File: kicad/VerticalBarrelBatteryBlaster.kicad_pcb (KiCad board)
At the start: 2 copper layers, 21.1 x 10.3 mm, 3 parts

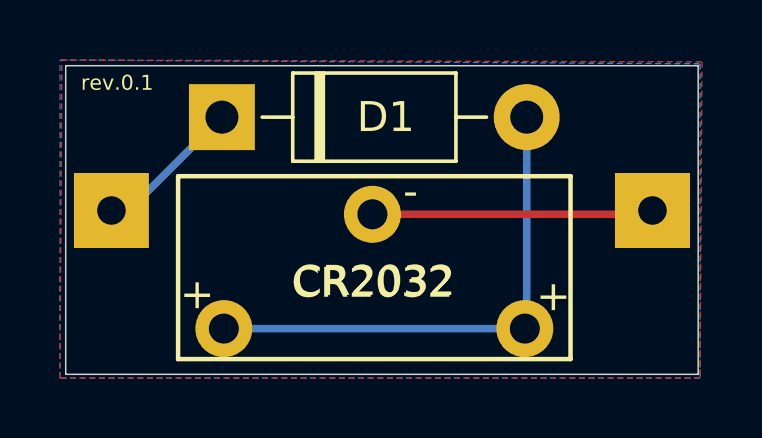
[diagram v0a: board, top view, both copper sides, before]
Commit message: Rev.0.2: Improves printed text
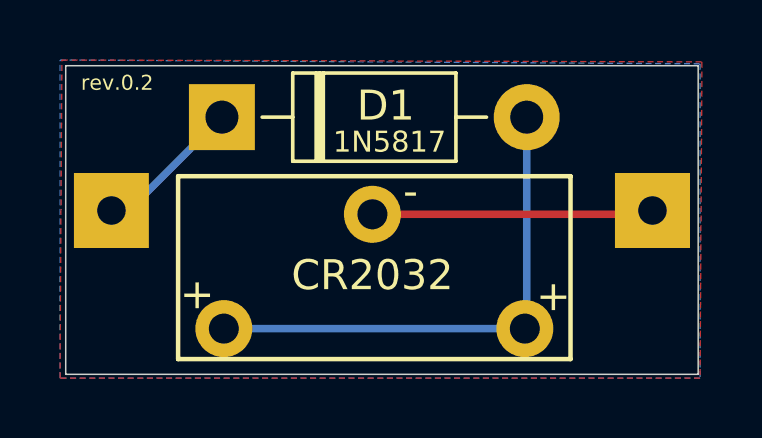
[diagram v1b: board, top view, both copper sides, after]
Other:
- board text added: "-"
- board text added: "1N5817"
- board text added: "rev.0.2"
- board text removed: "rev.0.1"
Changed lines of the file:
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@@
   (general
     (thickness 1.6)
-    (drawings 124)
+    (drawings 126)
     (tracks 7)
     (zones 0)
@@
     (descr "Diode, DO-41_SOD81 series, Axial, Horizontal, pin pitch=10.16mm, , length*diameter=5.2*2.7mm^2, , http://www.diodes.com/_files/packages/DO-41%20(Plastic).pdf")
     (tags "Diode DO-41_SOD81 series Axial Horizontal pin pitch 10.16mm  length 5.2mm diameter 2.7mm")
-    (fp_text reference D1 (at 5.461 0) (layer F.SilkS)
+    (fp_text reference D1 (at 5.461 -0.381) (layer F.SilkS)
       (effects (font (size 1 1) (thickness 0.15)))
     )
@@
       (effects (font (size 1 1) (thickness 0.15)))
     )
+    (fp_line (start 2.48 -1.35) (end 2.48 1.35) (layer F.Fab) (width 0.1))
+    (fp_line (start 2.48 1.35) (end 7.68 1.35) (layer F.Fab) (width 0.1))
+    (fp_line (start 7.68 1.35) (end 7.68 -1.35) (layer F.Fab) (width 0.1))
+    (fp_line (start 7.68 -1.35) (end 2.48 -1.35) (layer F.Fab) (width 0.1))
+    (fp_line (start 0 0) (end 2.48 0) (layer F.Fab) (width 0.1))
+    (fp_line (start 10.16 0) (end 7.68 0) (layer F.Fab) (width 0.1))
+    (fp_line (start 3.26 -1.35) (end 3.26 1.35) (layer F.Fab) (width 0.1))
+    (fp_line (start 3.36 -1.35) (end 3.36 1.35) (layer F.Fab) (width 0.1))
+    (fp_line (start 3.16 -1.35) (end 3.16 1.35) (layer F.Fab) (width 0.1))
+    (fp_line (start 2.36 -1.47) (end 2.36 1.47) (layer F.SilkS) (width 0.12))
+    (fp_line (start 2.36 1.47) (end 7.8 1.47) (layer F.SilkS) (width 0.12))
+    (fp_line (start 7.8 1.47) (end 7.8 -1.47) (layer F.SilkS) (width 0.12))
+    (fp_line (start 7.8 -1.47) (end 2.36 -1.47) (layer F.SilkS) (width 0.12))
+    (fp_line (start 1.34 0) (end 2.36 0) (layer F.SilkS) (width 0.12))
+    (fp_line (start 8.82 0) (end 7.8 0) (layer F.SilkS) (width 0.12))
+    (fp_line (start 3.26 -1.47) (end 3.26 1.47) (layer F.SilkS) (width 0.12))
+    (fp_line (start 3.38 -1.47) (end 3.38 1.47) (layer F.SilkS) (width 0.12))
+    (fp_line (start 3.14 -1.47) (end 3.14 1.47) (layer F.SilkS) (width 0.12))
+    (fp_line (start -1.35 -1.6) (end -1.35 1.6) (layer F.CrtYd) (width 0.05))
+    (fp_line (start -1.35 1.6) (end 11.51 1.6) (layer F.CrtYd) (width 0.05))
+    (fp_line (start 11.51 1.6) (end 11.51 -1.6) (layer F.CrtYd) (width 0.05))
     (fp_line (start 11.51 -1.6) (end -1.35 -1.6) (layer F.CrtYd) (width 0.05))
-    (fp_line (start 11.51 1.6) (end 11.51 -1.6) (layer F.CrtYd) (width 0.05))
-    (fp_line (start -1.35 1.6) (end 11.51 1.6) (layer F.CrtYd) (width 0.05))
-    (fp_line (start -1.35 -1.6) (end -1.35 1.6) (layer F.CrtYd) (width 0.05))
-    (fp_line (start 3.14 -1.47) (end 3.14 1.47) (layer F.SilkS) (width 0.12))
-    (fp_line (start 3.38 -1.47) (end 3.38 1.47) (layer F.SilkS) (width 0.12))
-    (fp_line (start 3.26 -1.47) (end 3.26 1.47) (layer F.SilkS) (width 0.12))
-    (fp_line (start 8.82 0) (end 7.8 0) (layer F.SilkS) (width 0.12))
-    (fp_line (start 1.34 0) (end 2.36 0) (layer F.SilkS) (width 0.12))
-    (fp_line (start 7.8 -1.47) (end 2.36 -1.47) (layer F.SilkS) (width 0.12))
-    (fp_line (start 7.8 1.47) (end 7.8 -1.47) (layer F.SilkS) (width 0.12))
-    (fp_line (start 2.36 1.47) (end 7.8 1.47) (layer F.SilkS) (width 0.12))
-    (fp_line (start 2.36 -1.47) (end 2.36 1.47) (layer F.SilkS) (width 0.12))
-    (fp_line (start 3.16 -1.35) (end 3.16 1.35) (layer F.Fab) (width 0.1))
-    (fp_line (start 3.36 -1.35) (end 3.36 1.35) (layer F.Fab) (width 0.1))
-    (fp_line (start 3.26 -1.35) (end 3.26 1.35) (layer F.Fab) (width 0.1))
-    (fp_line (start 10.16 0) (end 7.68 0) (layer F.Fab) (width 0.1))
-    (fp_line (start 0 0) (end 2.48 0) (layer F.Fab) (width 0.1))
-    (fp_line (start 7.68 -1.35) (end 2.48 -1.35) (layer F.Fab) (width 0.1))
-    (fp_line (start 7.68 1.35) (end 7.68 -1.35) (layer F.Fab) (width 0.1))
-    (fp_line (start 2.48 1.35) (end 7.68 1.35) (layer F.Fab) (width 0.1))
-    (fp_line (start 2.48 -1.35) (end 2.48 1.35) (layer F.Fab) (width 0.1))
     (fp_text user K (at -1.5875 -3.937) (layer F.SilkS) hide
       (effects (font (size 1 1) (thickness 0.15)))
@@
       (effects (font (size 1 1) (thickness 0.15)))
     )
-    (fp_text user %R (at 5.47 0) (layer F.Fab)
+    (fp_text user %R (at 5.47 -0.5715) (layer F.Fab)
       (effects (font (size 1 1) (thickness 0.15)))
     )
@@
   (module VerticalBarrelBatteryBlaster:cr2032_vertical_battery_holder (layer F.Cu)
     (at 165.5445 87.884)
-    (fp_text reference CR2032 (at 5.0165 -1.5875) (layer F.SilkS)
+    (fp_text reference CR2032 (at 4.953 -1.778) (layer F.SilkS)
       (effects (font (size 1 1) (thickness 0.15)))
     )
@@
       (effects (font (size 1 1) (thickness 0.15)))
     )
+    (fp_line (start 11.811 -5.334) (end 11.811 1.27) (layer F.CrtYd) (width 0.12))
+    (fp_line (start 11.811 1.27) (end -1.778 1.27) (layer F.CrtYd) (width 0.12))
+    (fp_line (start -1.524 -5.08) (end 11.557 -5.08) (layer F.SilkS) (width 0.15))
+    (fp_line (start 11.557 -5.08) (end 11.557 1.016) (layer F.SilkS) (width 0.15))
+    (fp_line (start -1.524 -5.08) (end -1.524 1.016) (layer F.SilkS) (width 0.15))
+    (fp_line (start -1.524 1.016) (end 11.557 1.016) (layer F.SilkS) (width 0.15))
+    (fp_line (start 11.811 -5.334) (end -1.778 -5.334) (layer F.CrtYd) (width 0.12))
     (fp_line (start -1.778 -5.334) (end -1.778 1.27) (layer F.CrtYd) (width 0.12))
-    (fp_line (start 11.811 -5.334) (end -1.778 -5.334) (layer F.CrtYd) (width 0.12))
-    (fp_line (start -1.524 1.016) (end 11.557 1.016) (layer F.SilkS) (width 0.15))
-    (fp_line (start -1.524 -5.08) (end -1.524 1.016) (layer F.SilkS) (width 0.15))
-    (fp_line (start 11.557 -5.08) (end 11.557 1.016) (layer F.SilkS) (width 0.15))
-    (fp_line (start -1.524 -5.08) (end 11.557 -5.08) (layer F.SilkS) (width 0.15))
-    (fp_line (start 11.811 1.27) (end -1.778 1.27) (layer F.CrtYd) (width 0.12))
-    (fp_line (start 11.811 -5.334) (end 11.811 1.27) (layer F.CrtYd) (width 0.12))
-    (fp_text user CR2032 (at 4.953 -1.524) (layer F.SilkS)
-      (effects (font (size 1 1) (thickness 0.15)))
-    )
     (fp_text user - (at 6.223 -4.572) (layer F.SilkS)
       (effects (font (size 1 1) (thickness 0.15)))
@@
       (effects (font (size 1 1) (thickness 0.15)) (justify mirror))
     )
+    (fp_text user + (at 18.034 2.413) (layer B.SilkS)
+      (effects (font (size 2 2) (thickness 0.3)) (justify mirror))
+    )
+    (fp_text user + (at 18.034 3.048) (layer F.Mask)
+      (effects (font (size 2 2) (thickness 0.3)))
+    )
     (fp_text user - (at 0.127 3.048) (layer F.Mask)
       (effects (font (size 2 2) (thickness 0.3)))
     )
-    (fp_text user + (at 18.034 3.048) (layer F.Mask)
-      (effects (font (size 2 2) (thickness 0.3)))
-    )
-    (fp_text user + (at 18.034 2.413) (layer B.SilkS)
-      (effects (font (size 2 2) (thickness 0.3)) (justify mirror))
-    )
+    (pad 2 thru_hole rect (at 0 0 90) (size 2.5 2.5) (drill 0.95) (layers *.Cu *.Mask)
+      (net 1 GND))
     (pad 1 thru_hole rect (at 18.034 0 180) (size 2.5 2.5) (drill 0.95) (layers *.Cu *.Mask)
       (net 3 VDiode))
-    (pad 2 thru_hole rect (at 0 0 90) (size 2.5 2.5) (drill 0.95) (layers *.Cu *.Mask)
-      (net 1 GND))
+  )
+  (gr_text 1N5817 (at 171.069 81.661) (layer F.SilkS)
+    (effects (font (size 0.7 0.7) (thickness 0.1)))
+  )
+  (gr_text - (at 179.7685 81.5975) (layer B.SilkS)
+    (effects (font (size 2 2) (thickness 0.3)) (justify mirror))
   )
   (gr_line (start 161.8615 88.138) (end 161.7345 87.9475) (layer F.Mask) (width 0.0692))
@@
   (gr_line (start 163.0045 87.757) (end 162.8775 87.503) (layer F.Mask) (width 0.0692))
   (gr_line (start 162.4965 87.122) (end 162.1155 87.122) (layer F.Mask) (width 0.0692))
-  (gr_text "Vertical\nBarrel\nBattery\nBlaster" (at 177.927 87.249) (layer F.Mask)
-    (effects (font (size 0.48 0.48) (thickness 0.08)) (justify left))
-  )
-  (gr_text rev.0.1 (at 161.9885 79.6925) (layer F.SilkS)
+  (gr_text "Vertical\nBarrel\nBattery\nBlaster" (at 164.1475 84.709) (layer F.Mask)
+    (effects (font (size 0.55 0.6) (thickness 0.09)) (justify left))
+  )
+  (gr_text rev.0.2 (at 161.9885 79.6925) (layer F.SilkS)
     (effects (font (size 0.5 0.5) (thickness 0.08)))
   )
-  (gr_text "by ScrapComputing" (at 170.561 88.265) (layer F.Mask)
-    (effects (font (size 0.5 0.5) (thickness 0.09)))
+  (gr_text "by\nScrapComputing" (at 170.6245 87.8205) (layer F.Mask)
+    (effects (font (size 0.6 0.6) (thickness 0.1)))
   )
   (gr_line (start 172.466 83.185) (end 168.148 79.883) (layer B.SilkS) (width 0.2))
@@
   (gr_line (start 172.085 82.296) (end 172.085 80.01) (layer B.SilkS) (width 0.12))
   (gr_line (start 172.212 83.312) (end 172.212 80.899) (layer B.SilkS) (width 0.15))
-  (gr_text rev.0.1 (at 179.2605 88.5825) (layer B.SilkS)
+  (gr_text rev.0.2 (at 179.2605 88.5825) (layer B.SilkS)
     (effects (font (size 0.8 0.8) (thickness 0.1)) (justify mirror))
   )
